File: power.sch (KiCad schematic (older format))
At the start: 36 parts, among them U18 MT9700, U19 MT9700, U20 MT9700, U21 TPS5430DDA, U22 MT3410L

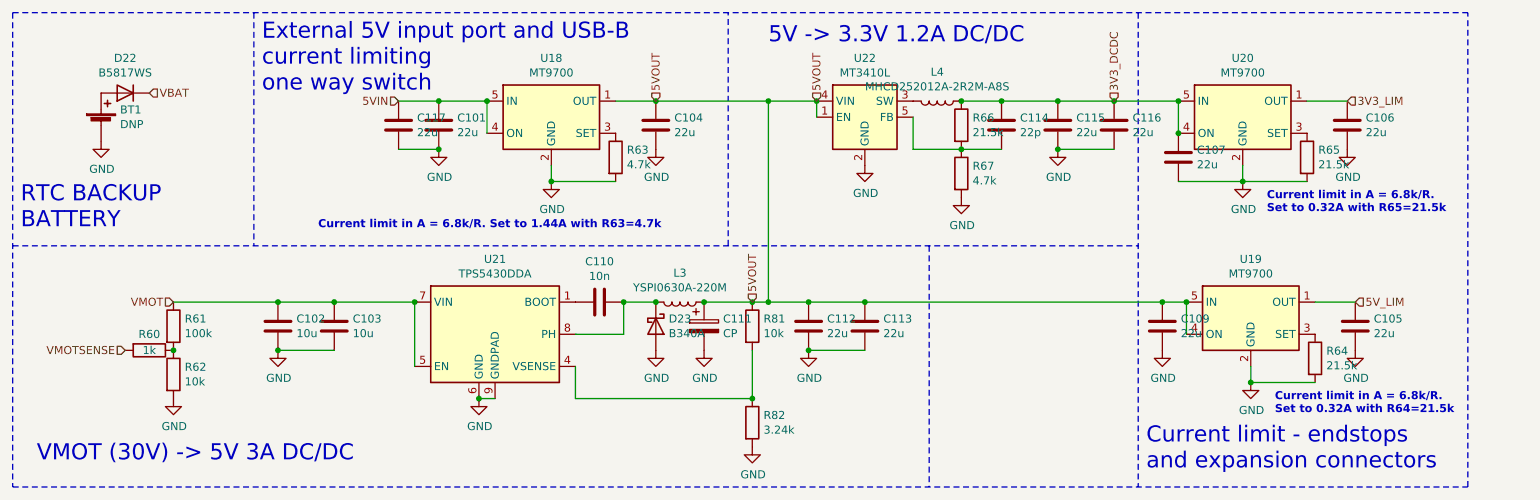
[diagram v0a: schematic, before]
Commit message: Fix flipped motor MOSFETS. Add reverse current block and current limit to 5V DC/DC supply. Add pullups to SD and card detect.
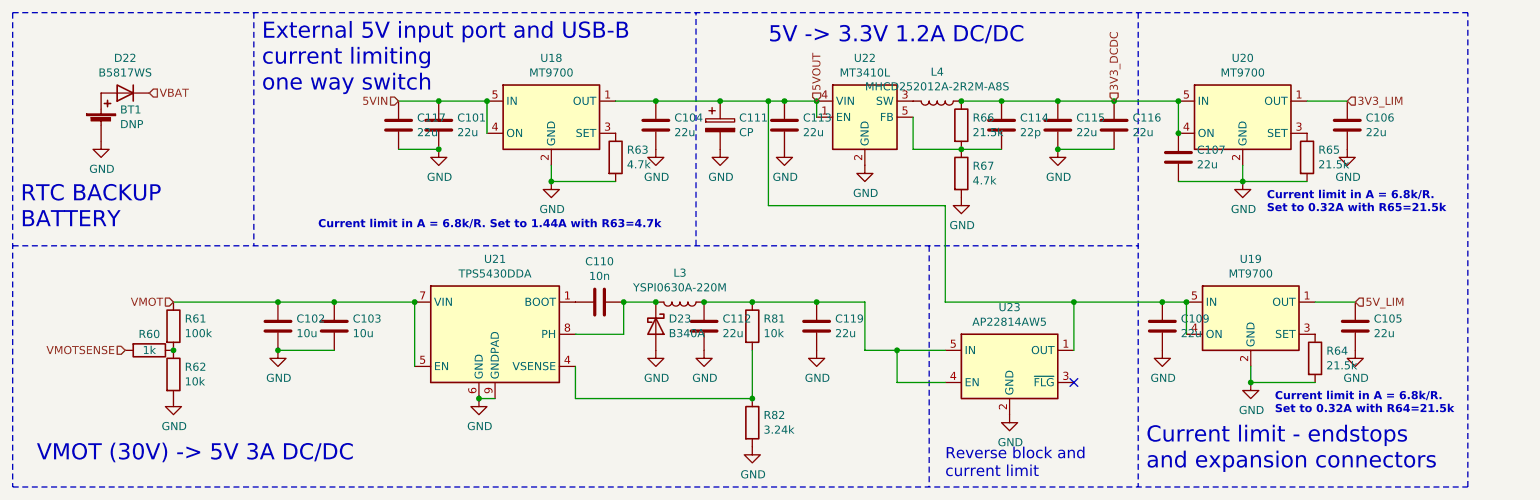
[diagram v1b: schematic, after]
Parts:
- added C119: 22u, Capacitor_SMD:C_0805_2012Metric, symbol Device:C
- added U23: AP22814AW5, Package_TO_SOT_SMD:SOT-23-5, symbol Power_Management:AP22814AW5
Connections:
- net 5VOUT: now also U23.1 (OUT); no longer C112.1, L3.1, R81.1
- net GND: now also C119.2, U23.2 (GND)
- new net: C112.1, C119.1, L3.1, R81.1, U23.4 (EN), U23.5 (IN)
- no-connect marks 0 -> 1
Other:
- note added: "Reverse block and \ncurrent limit"
- moved on the sheet: C111, C112, C113
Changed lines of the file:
@@
 Text HLabel 3150 2700 0    50   Input ~ 0
 5VIN
-Text HLabel 4750 2700 1    50   Input ~ 0
-5VOUT
 Text HLabel 1750 3950 0    50   Input ~ 0
 VMOT
@@
 L Device:CP C111
 U 1 1 63D04F5F
-P 5050 4100
-F 0 "C111" H 5168 4146 50  0000 L CNN
-F 1 "CP" H 5168 4055 50  0000 L CNN
-F 2 "Capacitor_SMD:CP_Elec_8x11.9" H 5088 3950 50  0001 C CNN
-F 3 "~" H 5050 4100 50  0001 C CNN
-	1    5050 4100
+P 5150 2850
+F 0 "C111" H 5268 2896 50  0000 L CNN
+F 1 "CP" H 5268 2805 50  0000 L CNN
+F 2 "Capacitor_SMD:CP_Elec_8x11.9" H 5188 2700 50  0001 C CNN
+F 3 "~" H 5150 2850 50  0001 C CNN
+	1    5150 2850
 	1    0    0    -1
 $EndComp
@@
 	1    0    0    -1
 $EndComp
-Wire Wire Line
-	5050 3950 5350 3950
 Connection ~ 5050 3950
 Wire Wire Line
@@
 	1    0    0    -1
 $EndComp
-Text HLabel 5350 3950 1    50   Input ~ 0
-5VOUT
 $Comp
 L Device:C C112
 U 1 1 63D0A6B7
-P 5700 4100
-F 0 "C112" H 5815 4146 50  0000 L CNN
-F 1 "22u" H 5815 4055 50  0000 L CNN
-F 2 "Capacitor_SMD:C_0805_2012Metric" H 5738 3950 50  0001 C CNN
-F 3 "~" H 5700 4100 50  0001 C CNN
-	1    5700 4100
-	1    0    0    -1
-$EndComp
-Wire Wire Line
-	5700 3950 5450 3950
-Connection ~ 5350 3950
-$Comp
-L power:GND #PWR?
-U 1 1 63D0B236
-P 5700 4250
-AR Path="/63D0B236" Ref="#PWR?"  Part="1"
-AR Path="/631D7D17/63D0B236" Ref="#PWR060"  Part="1"
-F 0 "#PWR060" H 5700 4000 50  0001 C CNN
-F 1 "GND" H 5705 4077 50  0000 C CNN
-F 2 "" H 5700 4250 50  0001 C CNN
-F 3 "" H 5700 4250 50  0001 C CNN
-	1    5700 4250
-	1    0    0    -1
-$EndComp
-$Comp
-L Device:C C113
-U 1 1 63D0B628
-P 6050 4100
-F 0 "C113" H 6165 4146 50  0000 L CNN
-F 1 "22u" H 6165 4055 50  0000 L CNN
-F 2 "Capacitor_SMD:C_0805_2012Metric" H 6088 3950 50  0001 C CNN
-F 3 "~" H 6050 4100 50  0001 C CNN
-	1    6050 4100
-	1    0    0    -1
-$EndComp
-Wire Wire Line
-	6050 3950 5700 3950
-Connection ~ 5700 3950
-Wire Wire Line
-	6050 4250 5700 4250
-Connection ~ 5700 4250
+P 5050 4100
+F 0 "C112" H 5165 4146 50  0000 L CNN
+F 1 "22u" H 5165 4055 50  0000 L CNN
+F 2 "Capacitor_SMD:C_0805_2012Metric" H 5088 3950 50  0001 C CNN
+F 3 "~" H 5050 4100 50  0001 C CNN
+	1    5050 4100
+	1    0    0    -1
+$EndComp
 $Comp
 L Diode:B340 D23
@@
 Connection ~ 7900 3950
 Wire Wire Line
-	5750 2700 5450 2700
-Wire Wire Line
-	5450 2700 5450 3950
+	5450 2700 5450 3350
 Connection ~ 5750 2700
-Connection ~ 5450 3950
-Wire Wire Line
-	5450 3950 5350 3950
-Wire Wire Line
-	6050 3950 7900 3950
-Connection ~ 6050 3950
-Wire Wire Line
-	5450 2700 4750 2700
-Connection ~ 5450 2700
 Connection ~ 4750 2700
 Wire Notes Line
 	6450 3600 6450 5100
 Wire Notes Line
-	5200 3600 5200 2150
+	5000 3600 5000 2150
 Wire Notes Line
 	2250 2150 2250 3600
@@
 Text Notes 8600 4650 0    50   ~ 10
 Current limit in A = 6.8k/R. \nSet to 0.32A with R64=21.5k
+$Comp
+L Power_Management:AP22814AW5 U23
+U 1 1 617F5F71
+P 6950 4350
+F 0 "U23" H 6950 4717 50  0000 C CNN
+F 1 "AP22814AW5" H 6950 4626 50  0000 C CNN
+F 2 "Package_TO_SOT_SMD:SOT-23-5" H 6950 3950 50  0001 C CNN
+F 3 "https://www.diodes.com/assets/Datasheets/AP22804_14.pdf" H 6950 4400 50  0001 C CNN
+	1    6950 4350
+	1    0    0    -1
+$EndComp
+Connection ~ 5450 2700
+Wire Wire Line
+	5450 2700 5150 2700
+$Comp
+L power:GND #PWR?
+U 1 1 61821889
+P 6950 4650
+AR Path="/61821889" Ref="#PWR?"  Part="1"
+AR Path="/631D7D17/61821889" Ref="#PWR0149"  Part="1"
+F 0 "#PWR0149" H 6950 4400 50  0001 C CNN
+F 1 "GND" H 6955 4477 50  0000 C CNN
+F 2 "" H 6950 4650 50  0001 C CNN
+F 3 "" H 6950 4650 50  0001 C CNN
+	1    6950 4650
+	1    0    0    -1
+$EndComp
+$Comp
+L Device:C C113
+U 1 1 63D0B628
+P 5550 2850
+F 0 "C113" H 5665 2896 50  0000 L CNN
+F 1 "22u" H 5665 2805 50  0000 L CNN
+F 2 "Capacitor_SMD:C_0805_2012Metric" H 5588 2700 50  0001 C CNN
+F 3 "~" H 5550 2850 50  0001 C CNN
+	1    5550 2850
+	1    0    0    -1
+$EndComp
+Connection ~ 5550 2700
+Wire Wire Line
+	5550 2700 5450 2700
+$Comp
+L power:GND #PWR?
+U 1 1 618914CF
+P 5550 3000
+AR Path="/618914CF" Ref="#PWR?"  Part="1"
+AR Path="/631D7D17/618914CF" Ref="#PWR0150"  Part="1"
+F 0 "#PWR0150" H 5550 2750 50  0001 C CNN
+F 1 "GND" H 5555 2827 50  0000 C CNN
+F 2 "" H 5550 3000 50  0001 C CNN
+F 3 "" H 5550 3000 50  0001 C CNN
+	1    5550 3000
+	1    0    0    -1
+$EndComp
+Connection ~ 5150 2700
+Wire Wire Line
+	5150 2700 4750 2700
+$Comp
+L power:GND #PWR?
+U 1 1 61896B7B
+P 5150 3000
+AR Path="/61896B7B" Ref="#PWR?"  Part="1"
+AR Path="/631D7D17/61896B7B" Ref="#PWR0151"  Part="1"
+F 0 "#PWR0151" H 5150 2750 50  0001 C CNN
+F 1 "GND" H 5155 2827 50  0000 C CNN
+F 2 "" H 5150 3000 50  0001 C CNN
+F 3 "" H 5150 3000 50  0001 C CNN
+	1    5150 3000
+	1    0    0    -1
+$EndComp
+Wire Wire Line
+	5550 2700 5750 2700
+Wire Wire Line
+	5450 3350 6550 3350
+Wire Wire Line
+	6550 3950 7350 3950
+Wire Wire Line
+	5050 3950 5350 3950
+Wire Wire Line
+	7350 4250 7350 3950
+Connection ~ 7350 3950
+Wire Wire Line
+	7350 3950 7900 3950
+Wire Wire Line
+	6550 3350 6550 3950
+Wire Wire Line
+	6550 4250 6250 4250
+Wire Wire Line
+	6050 4250 6050 3950
+Wire Wire Line
+	6050 3950 5750 3950
+Connection ~ 5350 3950
+Wire Wire Line
+	6550 4450 6250 4450
+Wire Wire Line
+	6250 4450 6250 4250
+Connection ~ 6250 4250
+Wire Wire Line
+	6250 4250 6050 4250
+NoConn ~ 7350 4450
+$Comp
+L Device:C C119
+U 1 1 617B65EB
+P 5750 4100
+F 0 "C119" H 5865 4146 50  0000 L CNN
+F 1 "22u" H 5865 4055 50  0000 L CNN
+F 2 "Capacitor_SMD:C_0805_2012Metric" H 5788 3950 50  0001 C CNN
+F 3 "~" H 5750 4100 50  0001 C CNN
+	1    5750 4100
+	1    0    0    -1
+$EndComp
+Connection ~ 5750 3950
+Wire Wire Line
+	5750 3950 5350 3950
+$Comp
+L power:GND #PWR?
+U 1 1 617B6DBC
+P 5750 4250
+AR Path="/617B6DBC" Ref="#PWR?"  Part="1"
+AR Path="/631D7D17/617B6DBC" Ref="#PWR060"  Part="1"
+F 0 "#PWR060" H 5750 4000 50  0001 C CNN
+F 1 "GND" H 5755 4077 50  0000 C CNN
+F 2 "" H 5750 4250 50  0001 C CNN
+F 3 "" H 5750 4250 50  0001 C CNN
+	1    5750 4250
+	1    0    0    -1
+$EndComp
+Text Notes 6550 5050 0    69   ~ 0
+Reverse block and \ncurrent limit
 $EndSCHEMATC

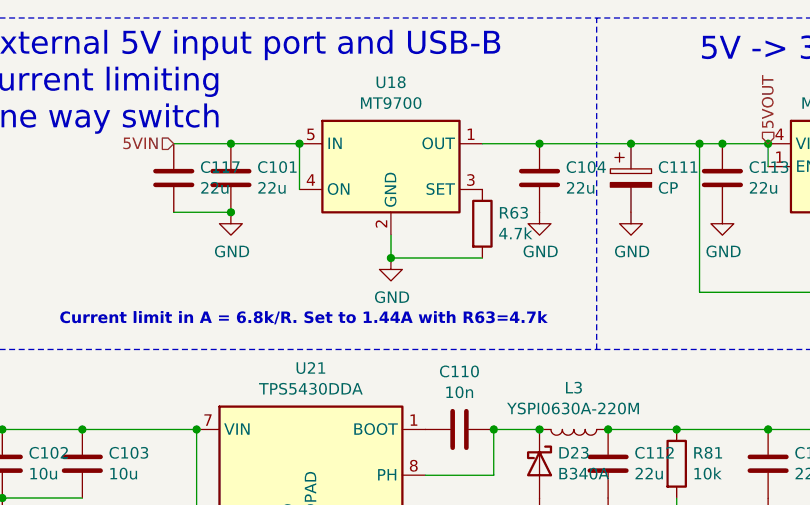
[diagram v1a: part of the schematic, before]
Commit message: Add solder jumper to disable 5Vin
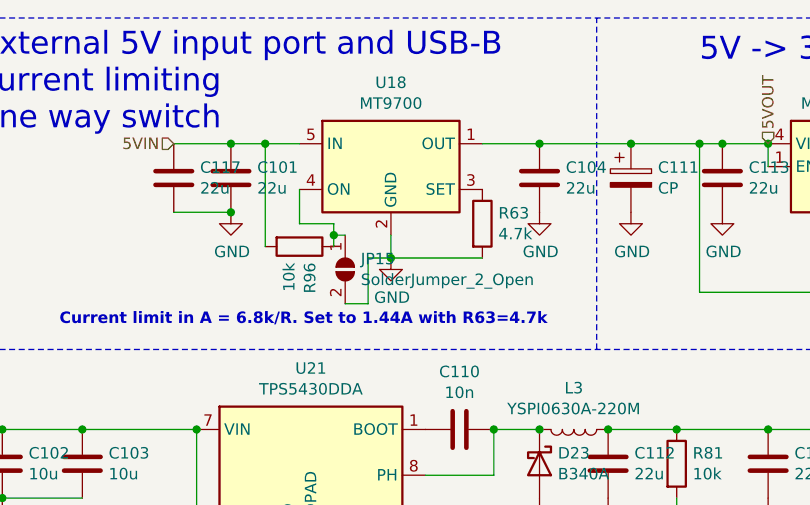
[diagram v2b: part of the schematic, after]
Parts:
- added JP15: SolderJumper_2_Open, Jumper:SolderJumper-2_P1.3mm_Open_TrianglePad1.0x1.5mm, symbol Jumper:SolderJumper_2_Open
- added R96: 10k, Resistor_SMD:R_0402_1005Metric, symbol Device:R
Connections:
- net 5VIN: now also R96.2; no longer U18.4 (ON)
- net GND: now also JP15.2 (B)
- new net: JP15.1 (A), R96.1, U18.4 (ON)
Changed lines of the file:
@@
 Connection ~ 4100 3200
 Wire Wire Line
-	3700 2700 3700 2900
-Wire Wire Line
-	3700 2700 3400 2700
-Connection ~ 3700 2700
+	3700 2700 3550 2700
 $Comp
 L Device:R R?
@@
 Text Notes 6550 5050 0    69   ~ 0
 Reverse block and \ncurrent limit
+$Comp
+L Device:R R?
+U 1 1 61894662
+P 3700 3150
+AR Path="/61894662" Ref="R?"  Part="1"
+AR Path="/631D7D17/61894662" Ref="R96"  Part="1"
+F 0 "R96" H 3770 3196 50  0000 L CNN
+F 1 "10k" H 3770 3105 50  0000 L CNN
+F 2 "Resistor_SMD:R_0402_1005Metric" V 3630 3150 50  0001 C CNN
+F 3 "~" H 3700 3150 50  0001 C CNN
+	1    3700 3150
+	0    1    1    0
+$EndComp
+Wire Wire Line
+	3850 3150 3850 3100
+Wire Wire Line
+	3850 3050 3700 3050
+Wire Wire Line
+	3700 3050 3700 2900
+Wire Wire Line
+	3550 3150 3550 2700
+Connection ~ 3550 2700
+Wire Wire Line
+	3550 2700 3400 2700
+$Comp
+L Jumper:SolderJumper_2_Open JP15
+U 1 1 61899F74
+P 3900 3250
+F 0 "JP15" V 3854 3318 50  0000 L CNN
+F 1 "SolderJumper_2_Open" V 3945 3318 50  0000 L CNN
+F 2 "Jumper:SolderJumper-2_P1.3mm_Open_TrianglePad1.0x1.5mm" H 3900 3250 50  0001 C CNN
+F 3 "~" H 3900 3250 50  0001 C CNN
+	1    3900 3250
+	0    1    1    0
+$EndComp
+Wire Wire Line
+	3900 3100 3850 3100
+Connection ~ 3850 3100
+Wire Wire Line
+	3850 3100 3850 3050
+Wire Wire Line
+	3900 3400 4000 3400
+Wire Wire Line
+	4000 3400 4000 3200
+Wire Wire Line
+	4000 3200 4100 3200
 $EndSCHEMATC

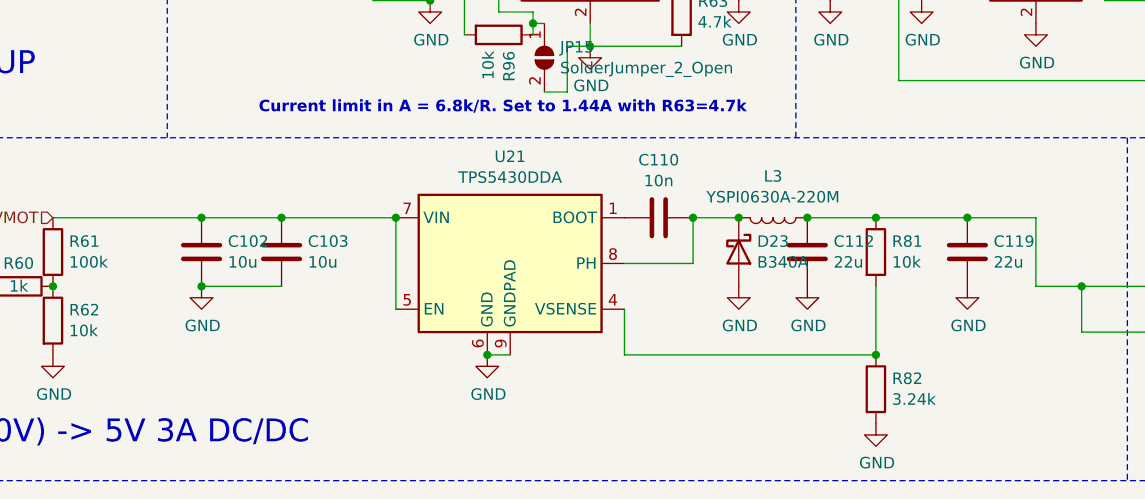
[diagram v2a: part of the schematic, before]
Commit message: Revision3 - Fix 5V cascading problem, change ADC opamp supply to 5V, add comparator to probe input, pulldown FETs when their MCU pins float.
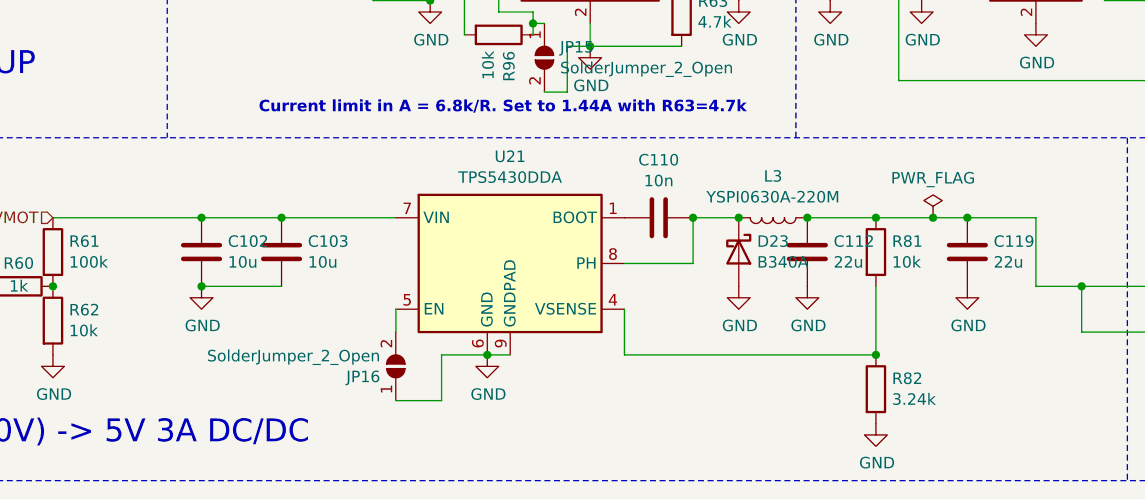
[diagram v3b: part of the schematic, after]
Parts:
- added JP16: SolderJumper_2_Open, Jumper:SolderJumper-2_P1.3mm_Open_TrianglePad1.0x1.5mm, symbol Jumper:SolderJumper_2_Open
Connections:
- net GND: now also JP16.1 (A)
- net VMOT: no longer U21.5 (EN)
- new net: JP16.2 (B), U21.5 (EN)
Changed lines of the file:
@@
 Text HLabel 7600 2700 1    50   Input ~ 0
 3V3_DCDC
-Wire Wire Line
-	3250 4350 3250 3950
-Connection ~ 3250 3950
 $Comp
 L Device:C C117
@@
 Connection ~ 5750 3950
 Wire Wire Line
-	5750 3950 5350 3950
+	5750 3950 5600 3950
 $Comp
 L power:GND #PWR?
@@
 Wire Wire Line
 	4000 3200 4100 3200
+$Comp
+L Jumper:SolderJumper_2_Open JP16
+U 1 1 61CF5C8F
+P 3250 4600
+F 0 "JP16" V 3204 4668 50  0000 L CNN
+F 1 "SolderJumper_2_Open" V 3295 4668 50  0000 L CNN
+F 2 "Jumper:SolderJumper-2_P1.3mm_Open_TrianglePad1.0x1.5mm" H 3250 4600 50  0001 C CNN
+F 3 "~" H 3250 4600 50  0001 C CNN
+	1    3250 4600
+	0    -1   -1   0
+$EndComp
+Wire Wire Line
+	3250 4450 3250 4350
+Wire Wire Line
+	3650 4550 3450 4550
+Wire Wire Line
+	3450 4550 3450 4750
+Wire Wire Line
+	3450 4750 3250 4750
+$Comp
+L power:PWR_FLAG #FLG0101
+U 1 1 61F941BB
+P 5600 3950
+F 0 "#FLG0101" H 5600 4025 50  0001 C CNN
+F 1 "PWR_FLAG" H 5600 4123 50  0000 C CNN
+F 2 "" H 5600 3950 50  0001 C CNN
+F 3 "~" H 5600 3950 50  0001 C CNN
+	1    5600 3950
+	1    0    0    -1
+$EndComp
+Connection ~ 5600 3950
+Wire Wire Line
+	5600 3950 5350 3950
 $EndSCHEMATC
